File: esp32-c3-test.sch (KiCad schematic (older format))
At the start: 31 parts, among them J1 Conn_01x03, J2 Conn_01x02, J3 Conn_01x01, J4 Conn_01x02, J5 Conn_01x02, J6 Conn_01x02, J9 USB_B_Micro, Q1 DTC143E, Q2 DTC143E, Q3 DTC143E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

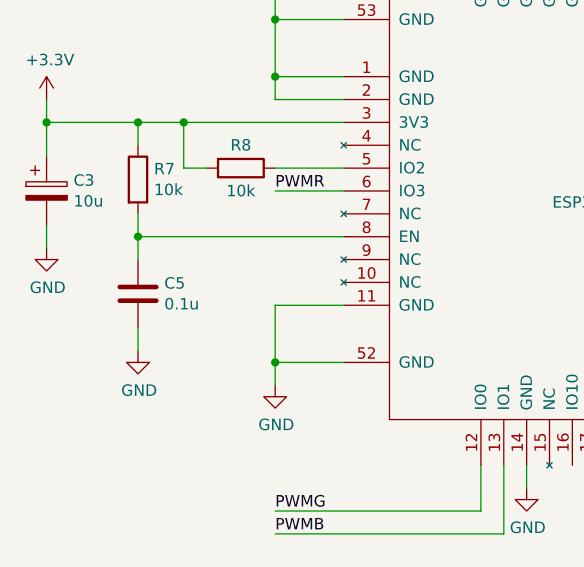
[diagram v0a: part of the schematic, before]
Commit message: 1. change c5 to c4 2. modify silkscreen of esp32-c3-mini-1 footprint to avoid via 3. move a few vias
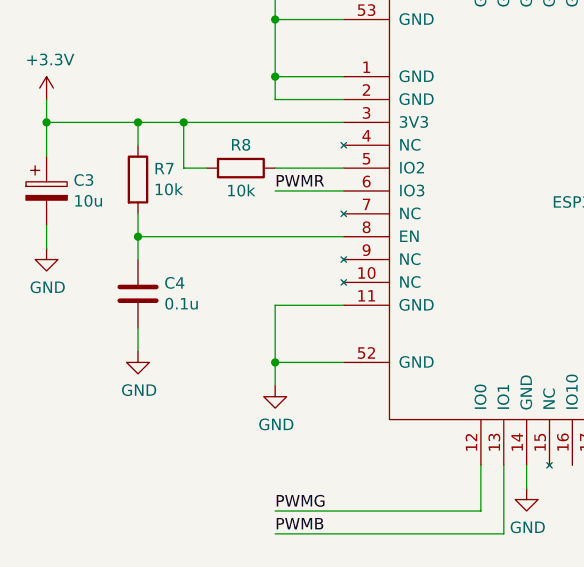
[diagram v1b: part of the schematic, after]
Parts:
- renumbered C5 to C4
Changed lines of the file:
@@
 	1600 2200 2300 2200
 $Comp
-L Device:C C5
+L Device:C C4
 U 1 1 61CDDCEA
 P 1400 2950
-F 0 "C5" H 1515 2996 50  0000 L CNN
+F 0 "C4" H 1515 2996 50  0000 L CNN
 F 1 "0.1u" H 1515 2905 50  0000 L CNN
 F 2 "Capacitor_SMD:C_0603_1608Metric_Pad1.08x0.95mm_HandSolder" H 1438 2800 50  0001 C CNN
